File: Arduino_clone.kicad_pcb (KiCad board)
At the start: 2 copper layers, 17 parts, among them J1 Conn_01x04, J2 DIGITAL PIN, J3 Conn_01x04, J4 icsp, U1 DS1337_ben, U2 24LC1025, U3 24LC1025, U4 ATmega328P-A, Y1 Crystal, Y2 Crystal

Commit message: layout on pcbnew
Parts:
- moved C2 78.2 mm to (119.2, 97.9)
- moved R2 75.2 mm to (114.6, 94.6), turned to 180 degrees
- moved C1 73.4 mm to (119.3, 101.7)
- moved Y2 68.5 mm to (114.2, 99.8), turned to 90 degrees
- moved R1 60.4 mm to (138.4, 114.2), turned to 180 degrees
- moved U4 56.1 mm to (118.8, 109.1)
- moved D1 55.5 mm to (144.1, 114.4)
- moved U2 55.4 mm to (130.3, 111.9)
- moved U3 55.3 mm to (130.3, 104.1)
- moved C3 49.6 mm to (138.2, 109.2), turned to 180 degrees
- moved Y1 38.7 mm to (143.5, 109.2)
- moved BT1 38.0 mm to (108.1, 99.3)
- moved U1 32.8 mm to (141.5, 102.3)
- moved J4 28.2 mm to (110.6, 107.5)
- moved J2 23.2 mm to (118.6, 118.6), turned to 90 degrees
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
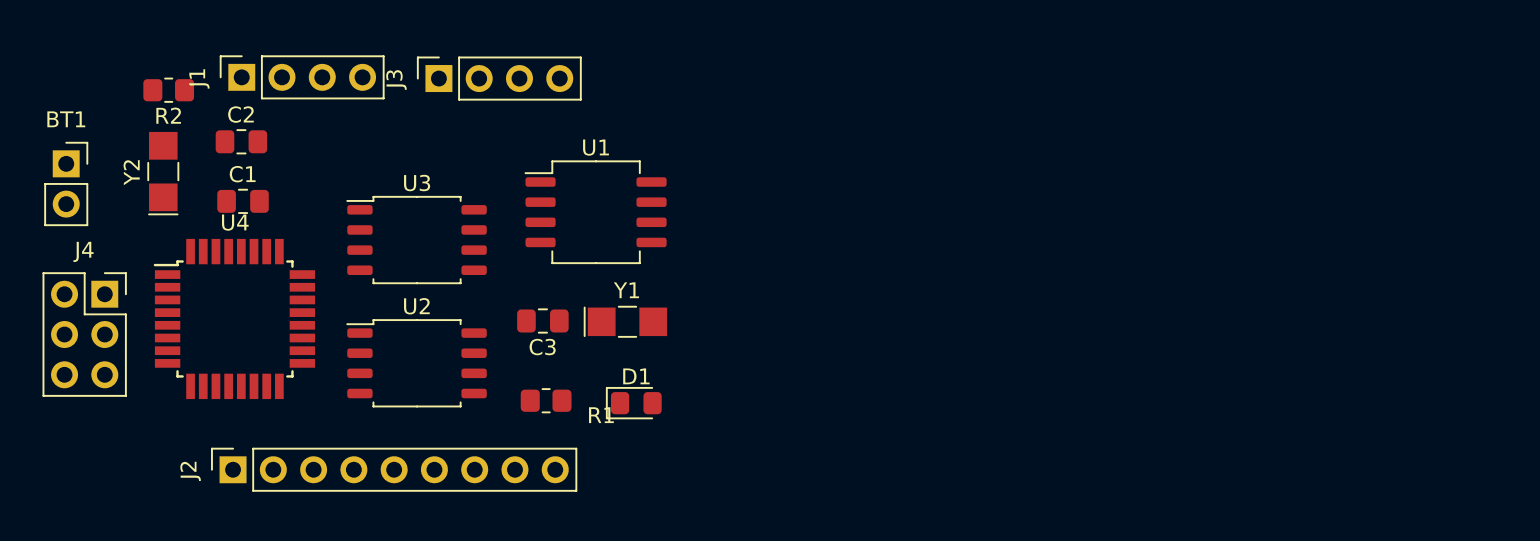
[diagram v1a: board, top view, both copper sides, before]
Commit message: created outline and mounting holes
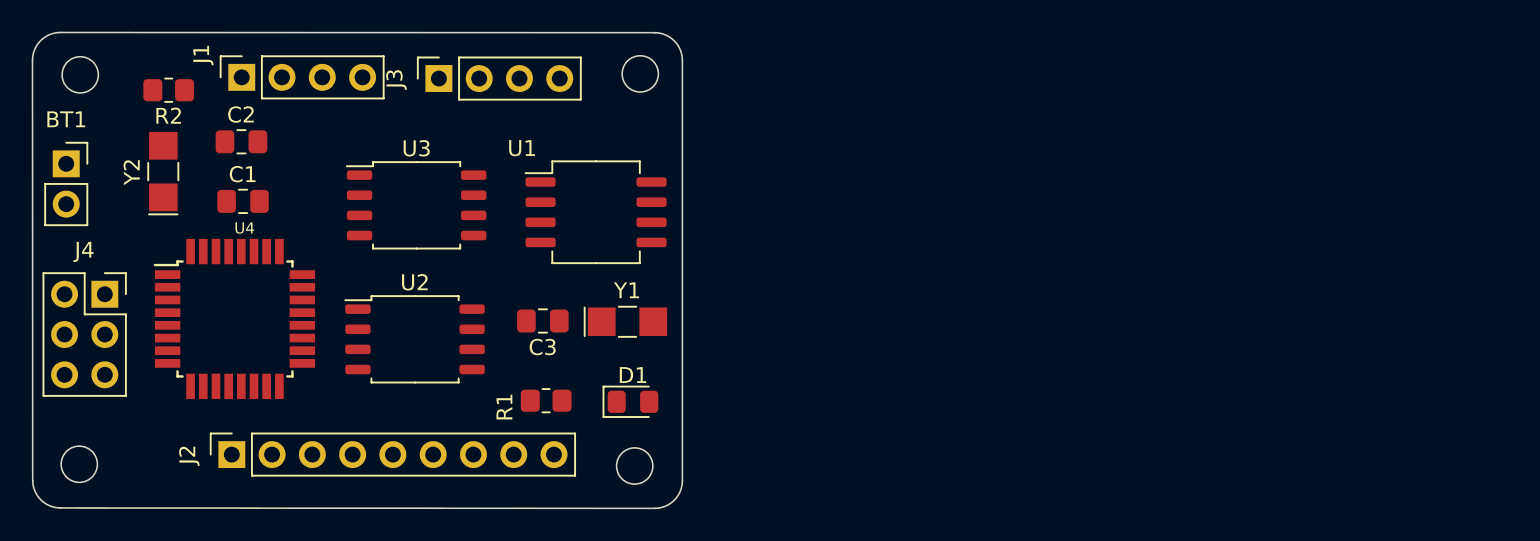
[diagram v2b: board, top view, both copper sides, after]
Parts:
- moved U3 2.19 mm to (130.2, 101.9)
- moved U2 1.52 mm to (130.1, 110.3)
- moved J2 0.96 mm to (118.6, 117.6)
- moved D1 0.23 mm to (143.9, 114.3)
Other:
- board outline added: 41 x 30 mm
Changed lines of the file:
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@@
   (net 33 "/connectors/VCC")
   (footprint "LED_SMD:LED_0805_2012Metric_Pad1.15x1.40mm_HandSolder" (layer "F.Cu")
-    (at 144.0828 114.3758)
+    (at 143.87 114.29)
     (descr "LED SMD 0805 (2012 Metric), square (rectangular) end terminal, IPC_7351 nominal, (Body size source: https://docs.google.com/spreadsheets/d/1BsfQQcO9C6DZCsRaXUlFlo91Tg2WpOkGARC1WS5S8t0/edit?usp=sharing), generated with kicad-footprint-generator")
     (tags "LED handsolder")
@@
   )
   (footprint "Package_SO:SOP-8_5.28x5.23mm_P1.27mm" (layer "F.Cu")
-    (at 130.2512 104.0892)
+    (at 130.225 101.9)
     (descr "SOP, 8 Pin (http://www.macronix.com/Lists/Datasheet/Attachments/7534/MX25R3235F,%20Wide%20Range,%2032Mb,%20v1.6.pdf#page=80), generated with kicad-footprint-generator ipc_gullwing_generator.py")
     (tags "SOP SO")
@@
     (property "Sheetname" "")
     (attr smd)
-    (fp_text reference "R1" (at -3.4852 -0.9478) (layer "F.SilkS")
+    (fp_text reference "R1" (at 2.5932 -0.4016 90) (layer "F.SilkS")
       (effects (font (size 1 1) (thickness 0.15)))
     )
@@
   )
   (footprint "Connector_PinSocket_2.54mm:PinSocket_1x09_P2.54mm_Vertical" (layer "F.Cu")
-    (at 118.6488 118.5762 90)
+    (at 118.57 117.62 90)
     (descr "Through hole straight socket strip, 1x09, 2.54mm pitch, single row (from Kicad 4.0.7), script generated")
     (tags "Through hole socket strip THT 1x09 2.54mm single row")
@@
       (effects (font (size 1 1) (thickness 0.15)))
     )
-    (fp_text value "DIGITAL PIN" (at 0 23.09 90) (layer "F.Fab")
+    (fp_text value "DIGITAL PIN" (at -2.2516 17.8254 180) (layer "F.Fab")
       (effects (font (size 1 1) (thickness 0.15)))
     )
@@
       (effects (font (size 1 1) (thickness 0.15)))
     )
-    (fp_text value "icsp" (at 2.2152 7.1478) (layer "F.Fab")
+    (fp_text value "icsp" (at -1.4108 7.5422) (layer "F.Fab")
       (effects (font (size 1 1) (thickness 0.15)))
     )
@@
       (effects (font (size 1 1) (thickness 0.15)))
     )
-    (fp_text value "C_Polarized 10uf" (at 0 1.68) (layer "F.Fab")
-      (effects (font (size 1 1) (thickness 0.15)))
+    (fp_text value "C_Polarized 10uf" (at 0.49 1.4442) (layer "F.Fab")
+      (effects (font (size 0.5 0.5) (thickness 0.125)))
     )
     (fp_text user "${REFERENCE}" (at 0 0) (layer "F.Fab")
@@
     (property "Sheetname" "")
     (attr smd)
-    (fp_text reference "U4" (at 0 -6.05) (layer "F.SilkS")
-      (effects (font (size 1 1) (thickness 0.15)))
-    )
-    (fp_text value "ATmega328P-A" (at 3.4852 5.3478) (layer "F.Fab")
+    (fp_text reference "U4" (at 0.6046 -5.7176) (layer "F.SilkS")
+      (effects (font (size 0.7 0.7) (thickness 0.15)))
+    )
+    (fp_text value "ATmega328P-A" (at 0.7046 6.0324) (layer "F.Fab")
       (effects (font (size 1 1) (thickness 0.15)))
     )
@@
       (effects (font (size 1 1) (thickness 0.15)))
     )
-    (fp_text value " 22pf" (at 0 1.68) (layer "F.Fab")
+    (fp_text value " 22pf" (at 2.6716 0.5992 90) (layer "F.Fab")
       (effects (font (size 1 1) (thickness 0.15)))
     )
@@
     (property "Sheetname" "connectors")
     (attr through_hole)
-    (fp_text reference "J1" (at 0 -2.77 90) (layer "F.SilkS")
-      (effects (font (size 1 1) (thickness 0.15)))
-    )
-    (fp_text value "Conn_01x04" (at -0.4572 7.7992 90) (layer "F.Fab")
+    (fp_text reference "J1" (at 1.4784 -2.5218 90) (layer "F.SilkS")
+      (effects (font (size 1 1) (thickness 0.15)))
+    )
+    (fp_text value "Conn_01x04" (at -1.7264 5.7712 180) (layer "F.Fab")
       (effects (font (size 1 1) (thickness 0.15)))
     )
@@
       (effects (font (size 1 1) (thickness 0.15)))
     )
-    (fp_text value "Battery 3v" (at 0 5.31) (layer "F.Fab")
+    (fp_text value "Battery 3v" (at 2.2476 0.4668 90) (layer "F.Fab")
       (effects (font (size 1 1) (thickness 0.15)))
     )
@@
       (effects (font (size 1 1) (thickness 0.15)))
     )
-    (fp_text value "Conn_01x04" (at -0.025 7.864 90) (layer "F.Fab")
+    (fp_text value "Conn_01x04" (at -1.549 5.6034 180) (layer "F.Fab")
       (effects (font (size 1 1) (thickness 0.15)))
     )
@@
   )
   (footprint "Package_SO:SOP-8_5.28x5.23mm_P1.27mm" (layer "F.Cu")
-    (at 130.2512 111.8616)
+    (at 130.125 110.35)
     (descr "SOP, 8 Pin (http://www.macronix.com/Lists/Datasheet/Attachments/7534/MX25R3235F,%20Wide%20Range,%2032Mb,%20v1.6.pdf#page=80), generated with kicad-footprint-generator ipc_gullwing_generator.py")
     (tags "SOP SO")
@@
       (effects (font (size 1 1) (thickness 0.15)))
     )
-    (fp_text value "24LC1025" (at 3.4852 2.8578) (layer "F.Fab")
+    (fp_text value "24LC1025" (at 0.2738 3.4134) (layer "F.Fab")
       (effects (font (size 1 1) (thickness 0.15)))
     )
@@
       (effects (font (size 1 1) (thickness 0.15)))
     )
-    (fp_text value "22pf" (at 0 1.68) (layer "F.Fab")
+    (fp_text value "22pf" (at 2.5482 0.0584 90) (layer "F.Fab")
       (effects (font (size 1 1) (thickness 0.15)))
     )
@@
     (property "Sheetname" "")
     (attr smd)
-    (fp_text reference "U1" (at 0 -4.05) (layer "F.SilkS")
-      (effects (font (size 1 1) (thickness 0.15)))
-    )
-    (fp_text value "DS1337_ben" (at 2.032 4.1516) (layer "F.Fab")
+    (fp_text reference "U1" (at -4.6622 -4.0128) (layer "F.SilkS")
+      (effects (font (size 1 1) (thickness 0.15)))
+    )
+    (fp_text value "DS1337_ben" (at 0.6822 -4.5612) (layer "F.Fab")
       (effects (font (size 1 1) (thickness 0.15)))
     )
@@
     )
   )
+  (gr_arc (start 107.762437 120.987563) (mid 106.538164 120.488189) (end 106.012437 119.275) (layer "Edge.Cuts") (width 0.1))
+  (gr_circle (center 108.95 118.23) (end 110 118.68) (layer "Edge.Cuts") (width 0.1) (fill none))
+  (gr_circle (center 143.98 118.34) (end 145.03 118.79) (layer "Edge.Cuts") (width 0.1) (fill none))
+  (gr_arc (start 146.987563 119.325) (mid 146.453125 120.521944) (end 145.237563 121.012563) (layer "Edge.Cuts") (width 0.1))
+  (gr_arc (start 106 92.75) (mid 106.512563 91.512563) (end 107.75 91) (layer "Edge.Cuts") (width 0.1))
+  (gr_line (start 107.762437 120.987563) (end 145.237563 121.012563) (layer "Edge.Cuts") (width 0.1))
+  (gr_circle (center 109.01 93.67) (end 110.06 94.12) (layer "Edge.Cuts") (width 0.1) (fill none))
+  (gr_line (start 146.987563 119.325) (end 146.987563 92.762437) (layer "Edge.Cuts") (width 0.1))
+  (gr_arc (start 145.237563 91.012437) (mid 146.475 91.525) (end 146.987563 92.762437) (layer "Edge.Cuts") (width 0.1))
+  (gr_line (start 145.237563 91.012437) (end 107.75 91) (layer "Edge.Cuts") (width 0.1))
+  (gr_line (start 106 92.75) (end 106.012437 119.275) (layer "Edge.Cuts") (width 0.1))
+  (gr_circle (center 144.33 93.61) (end 145.38 94.06) (layer "Edge.Cuts") (width 0.1) (fill none))
 )
